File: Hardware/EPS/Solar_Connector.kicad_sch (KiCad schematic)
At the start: 4 parts, among them J701 Conn_01x02

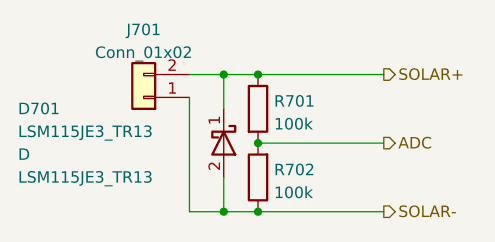
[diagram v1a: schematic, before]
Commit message: Updated to KiCAD 7.0
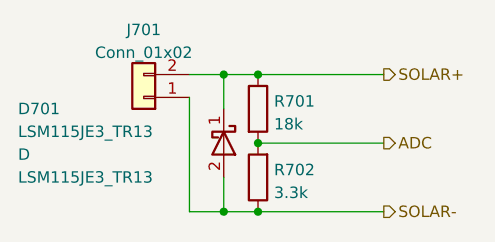
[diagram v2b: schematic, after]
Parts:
- R701: value 100k -> 18k
- R702: value 100k -> 3.3k
